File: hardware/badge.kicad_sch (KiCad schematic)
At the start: 2 parts

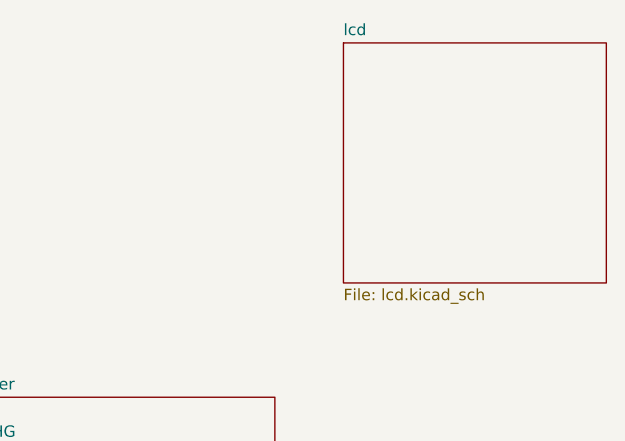
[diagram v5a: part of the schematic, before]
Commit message: Initial schema of LCD interface
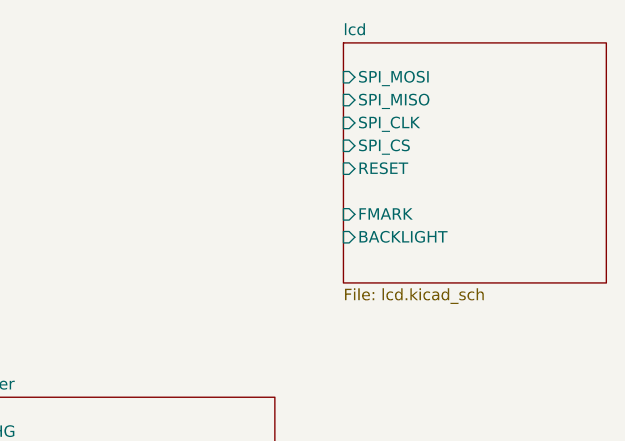
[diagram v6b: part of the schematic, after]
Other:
- sheet lcd ports: added BACKLIGHT, FMARK, RESET, SPI_CLK, SPI_CS, SPI_MISO, SPI_MOSI; removed none
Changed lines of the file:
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@@
+			)
+		)
+		(pin "RESET" input
+			(at 220.98 60.96 180)
+			(effects
+				(font
+					(size 1.27 1.27)
+				)
+				(justify left)
+			)
+		)
+		(pin "SPI_MOSI" input
+			(at 220.98 50.8 180)
+			(effects
+				(font
+					(size 1.27 1.27)
+				)
+				(justify left)
+			)
+		)
+		(pin "SPI_MISO" input
+			(at 220.98 53.34 180)
+			(effects
+				(font
+					(size 1.27 1.27)
+				)
+				(justify left)
+			)
+		)
+		(pin "SPI_CLK" input
+			(at 220.98 55.88 180)
+			(effects
+				(font
+					(size 1.27 1.27)
+				)
+				(justify left)
+			)
+		)
+		(pin "SPI_CS" input
+			(at 220.98 58.42 180)
+			(effects
+				(font
+					(size 1.27 1.27)
+				)
+				(justify left)
+			)
+		)
+		(pin "FMARK" input
+			(at 220.98 66.04 180)
+			(effects
+				(font
+					(size 1.27 1.27)
+				)
+				(justify left)
+			)
+		)
+		(pin "BACKLIGHT" input
+			(at 220.98 68.58 180)
+			(effects
+				(font
+					(size 1.27 1.27)
+				)
+				(justify left)
 			)
 		)

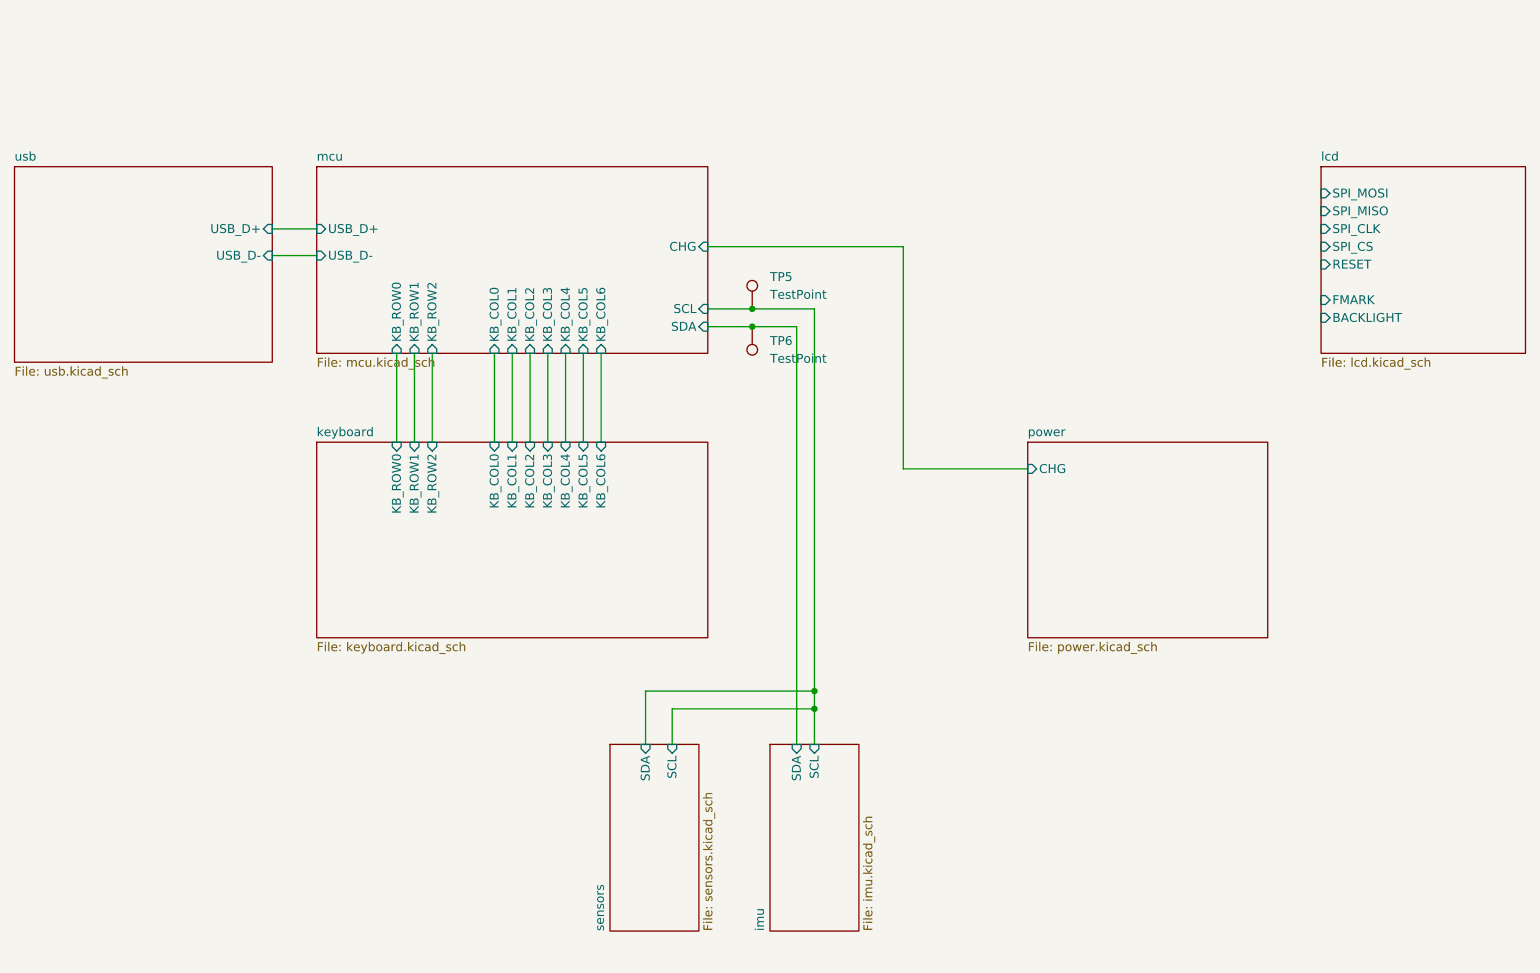
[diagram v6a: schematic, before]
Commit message: lcd wires, wire direction
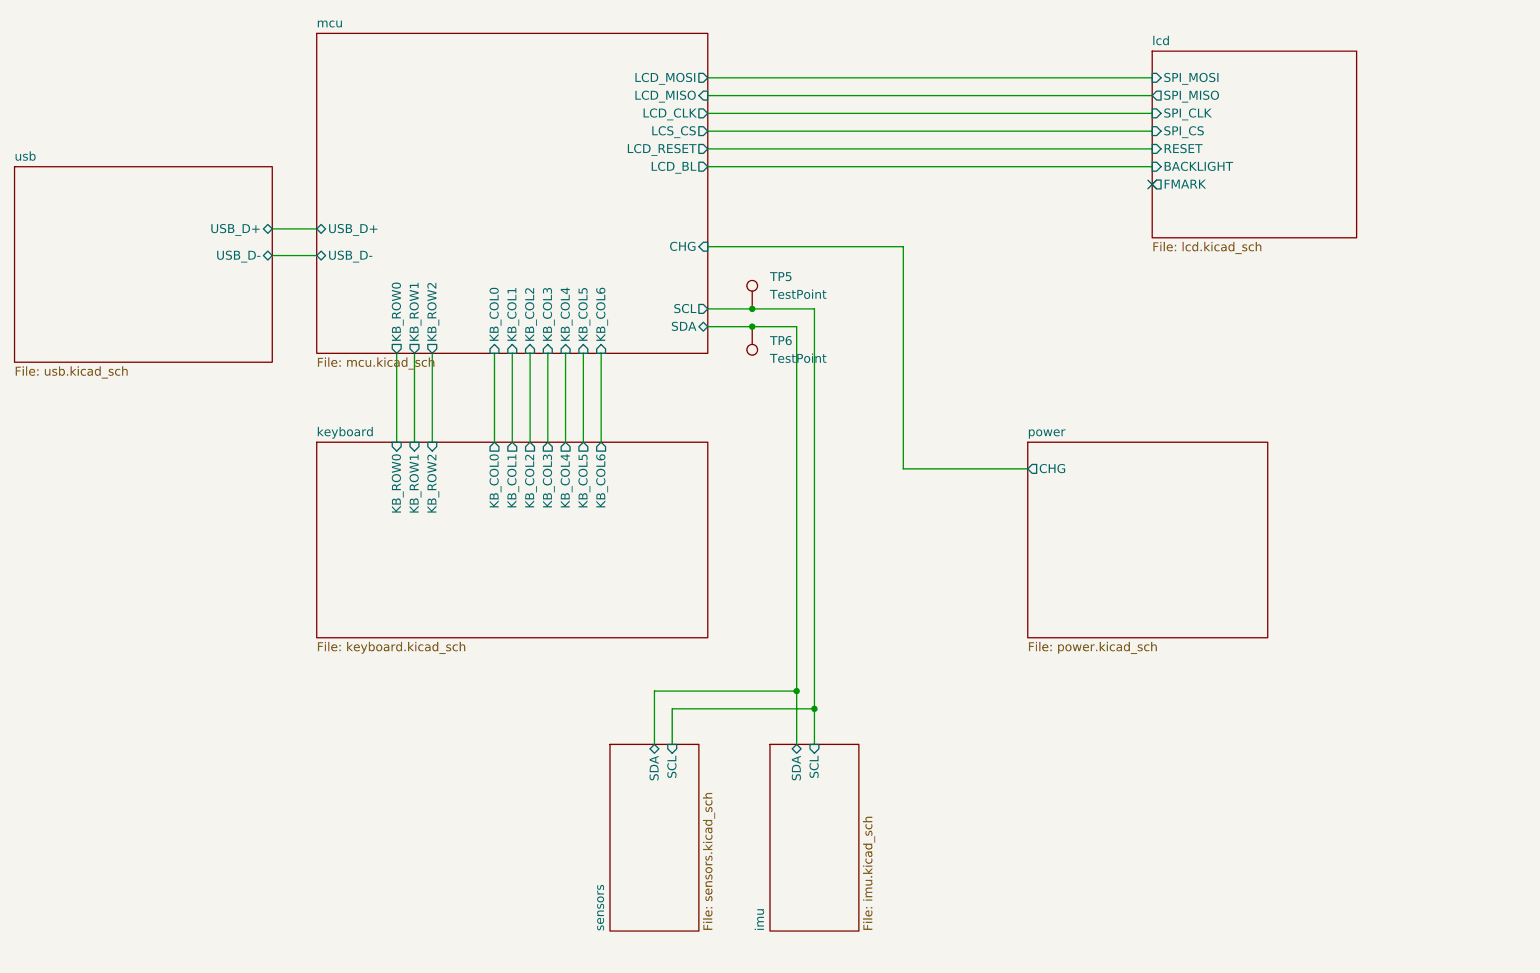
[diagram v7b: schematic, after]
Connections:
- no-connect marks 0 -> 1
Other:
- sheet mcu ports: added LCD_BL, LCD_CLK, LCD_MISO, LCD_MOSI, LCD_RESET, LCS_CS; removed none

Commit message: battery voltage divider
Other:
- sheet mcu ports: added VBAT_DIV2; removed none
- sheet power ports: added VBAT_DIV2; removed none
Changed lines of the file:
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@@
+	(wire
+		(pts
+			(xy 158.75 60.96) (xy 158.75 69.85)
+		)
+		(stroke
+			(width 0)
+			(type default)
+		)
+	)
 	(wire
 		(pts
@@
 	(wire
 		(pts
+			(xy 133.35 60.96) (xy 158.75 60.96)
+		)
+		(stroke
+			(width 0)
+			(type default)
+		)
+	)
+	(wire
+		(pts
 			(xy 115.57 73.66) (xy 115.57 86.36)
 		)
@@
 	(wire
 		(pts
+			(xy 158.75 69.85) (xy 180.34 69.85)
+		)
+		(stroke
+			(width 0)
+			(type default)
+		)
+	)
+	(wire
+		(pts
 			(xy 133.35 67.31) (xy 139.7 67.31)
 		)
@@
 	(wire
 		(pts
-			(xy 161.29 90.17) (xy 179.07 90.17)
+			(xy 161.29 67.31) (xy 180.34 67.31)
 		)
 		(stroke
@@
 	(wire
 		(pts
-			(xy 161.29 58.42) (xy 161.29 90.17)
+			(xy 161.29 58.42) (xy 161.29 67.31)
 		)
 		(stroke
@@
 			)
 		)
+		(pin "VBAT_DIV2" input
+			(at 133.35 60.96 0)
+			(effects
+				(font
+					(size 1.27 1.27)
+				)
+				(justify right)
+			)
+		)
 		(instances
 			(project "badge"
@@
 	)
 	(sheet
-		(at 179.07 86.36)
+		(at 180.34 64.77)
 		(size 34.29 27.94)
 		(fields_autoplaced yes)
@@
 		)
 		(property "Sheetname" "power"
-			(at 179.07 85.6484 0)
+			(at 180.34 64.0584 0)
 			(effects
 				(font
@@
 		)
 		(property "Sheetfile" "power.kicad_sch"
-			(at 179.07 114.8846 0)
+			(at 180.34 93.2946 0)
 			(effects
 				(font
@@
 		)
 		(pin "CHG" output
-			(at 179.07 90.17 180)
-			(effects
-				(font
+			(at 180.34 67.31 180)
+			(effects
+				(font
+					(size 1.27 1.27)
+				)
+				(justify left)
+			)
+		)
+		(pin "VBAT_DIV2" output
+			(at 180.34 69.85 180)
+			(effects
+				(font
